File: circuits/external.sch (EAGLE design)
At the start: 4 parts, among them T1 BC547B

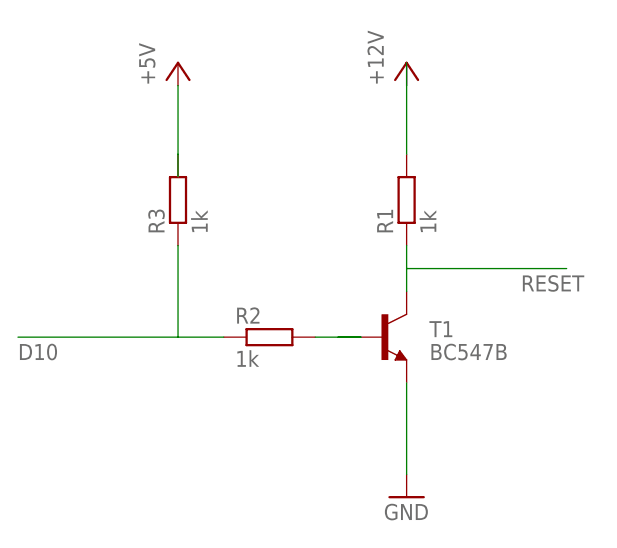
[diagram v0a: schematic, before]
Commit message: More documentation, started HVPP docs
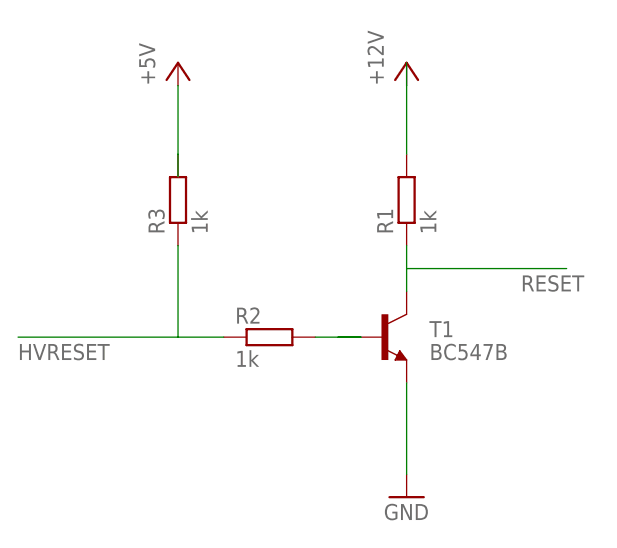
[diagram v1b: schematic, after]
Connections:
- net D10 renamed HVRESET
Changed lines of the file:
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@@
 </segment>
 </net>
-<net name="D10" class="0">
+<net name="HVRESET" class="0">
 <segment>
 <pinref part="R2" gate="G$1" pin="1"/>
